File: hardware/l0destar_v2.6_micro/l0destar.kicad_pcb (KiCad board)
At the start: 4 copper layers, 65.4 x 34.4 mm, 75 parts

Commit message: added v2.6C board, minor silkscreen tweaks to other PCBs
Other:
- board text removed: "120Ω"
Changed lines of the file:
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@@
 		)
 	)
-	(gr_text "120Ω"
-		(at 56.22 78 0)
+	(gr_text "GND"
+		(at 31.53 93.58 90)
 		(layer "B.SilkS")
 		(effects
@@
 				(size 0.8 0.8)
 				(thickness 0.15)
-				(bold yes)
 			)
 			(justify left bottom mirror)
+		)
+	)
+	(gr_text "4.2V"
+		(at 31.53 96.1 90)
+		(layer "B.SilkS")
+		(effects
+			(font
+				(size 0.8 0.8)
+				(thickness 0.15)
+			)
+			(justify left bottom mirror)

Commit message: minor PCB layout tweaks
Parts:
- moved S13D1 17.3 mm to (81.0, 106.2), turned to 90 degrees
- moved S13D2 17.3 mm to (82.7, 106.2), turned to 90 degrees
- moved S13D3 17.3 mm to (84.3, 106.2), turned to 90 degrees
- moved S13R1 12.1 mm to (76.4, 103.7), turned to 180 degrees
- moved S13R2 11.2 mm to (76.4, 102.7), turned to 180 degrees
- moved S13R3 10.5 mm to (76.4, 101.6), turned to 180 degrees
- moved H4 1.38 mm to (88.0, 106.3)
- moved H2 1.34 mm to (71.8, 77.2)
- moved S15C1 1.29 mm to (79.8, 81.2)
- moved S15C3 1.29 mm to (78.9, 85.0)
- moved S15FB1 1.29 mm to (77.8, 85.0)
- moved S15J1 1.29 mm to (76.6, 80.7)
- moved S15U1 1.29 mm to (75.0, 85.0)
- moved S15C2 1.29 mm to (80.0, 85.0)
- moved S15C4 1.29 mm to (81.1, 85.0)
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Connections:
- S1J2 pad 18: unconnected-(S1J2-Pin_18-Pad18) -> LED3
- S1J2 pad 19: unconnected-(S1J2-Pin_19-Pad19) -> LED2
- S1J2 pad 20: unconnected-(S1J2-Pin_20-Pad20) -> LED1
- S1J3 pad 21: LED1 -> unconnected-(S1J3-Pin_20-Pad21)
- S1J3 pad 22: LED2 -> unconnected-(S1J3-Pin_19-Pad22)
- S1J3 pad 23: LED3 -> unconnected-(S1J3-Pin_18-Pad23)
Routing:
- net Net-(S13D3-A): track 15.3 -> 8.93 mm
- net Net-(S13D2-A): track 12.2 -> 6.88 mm
- net GND: track 76.6 -> 71.9 mm, vias 125 -> 127
- net Net-(S13D1-A): track 8.79 -> 4.83 mm
- net LED3: track 3.32 -> 6.76 mm
- net PP3V3_GPS: track 19.0 -> 20.3 mm
- net LED2: track 3.21 -> 4.44 mm
- net PP3V3_AUX: track 23.2 -> 24.2 mm
- net LED1: track 3.04 -> 2.51 mm
- net unconnected-(S1J3-Pin_19-Pad22): track 0.00 -> 0.51 mm
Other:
- board size 65.4 x 34.4 mm -> 66.8 x 34.4 mm

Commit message: tweaked layouts
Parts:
- removed S1R3: 100K, Resistor_SMD:R_0402_1005Metric
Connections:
- S1J2 pad 2: VSYS -> unconnected-(S1J2-VSYS-Pad2)
- S1J2 pad 4: Net-(S1J2-ENABLE) -> unconnected-(S1J2-ENABLE-Pad4)
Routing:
- net Net-(S1J2-ENABLE): track 3.54 -> 0.00 mm
- net VSYS: track 3.07 -> 0.00 mm
- net GND: track 71.9 -> 71.6 mm, vias 127 -> 113
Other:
- board text removed: "ENABLE"
- board text removed: "VSYS"

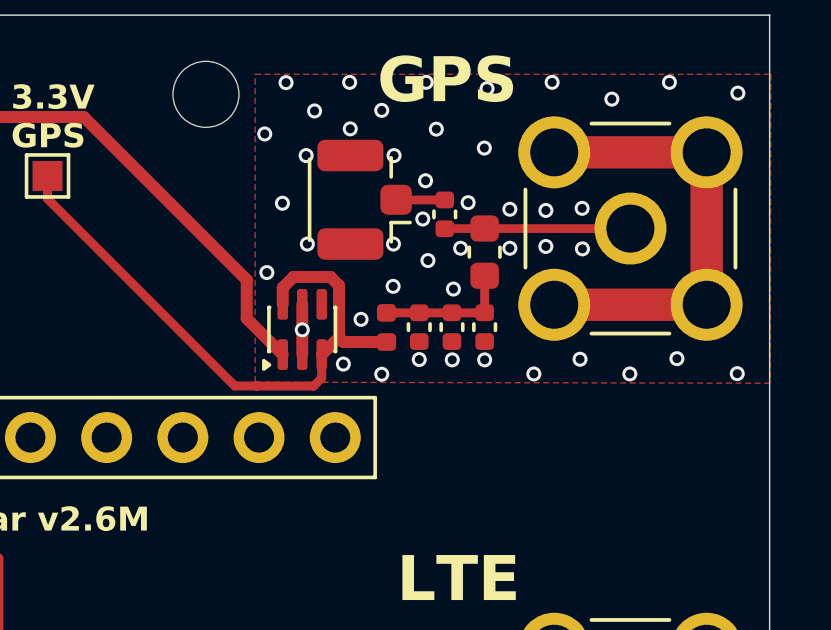
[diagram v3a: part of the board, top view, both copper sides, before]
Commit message: fix bias tee cap ordering on all boards
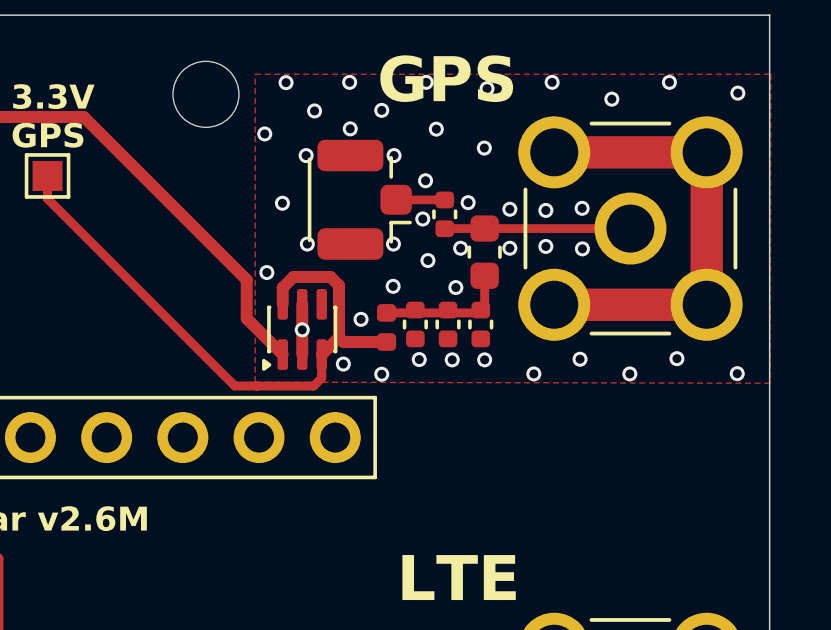
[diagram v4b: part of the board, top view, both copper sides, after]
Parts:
- moved S15C4 2.31 mm to (78.8, 84.9)
- moved S15C2 0.96 mm to (81.0, 84.9)
- moved S15C3 0.96 mm to (79.9, 84.9)
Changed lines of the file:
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@@
 	(footprint "Capacitor_SMD:C_0402_1005Metric"
 		(layer "F.Cu")
-		(at 78.9 84.97 -90)
+		(at 79.86 84.88 -90)
 		(descr "Capacitor SMD 0402 (1005 Metric), square (rectangular) end terminal, IPC-7351 nominal, (Body size source: IPC-SM-782 page 76, https://www.pcb-3d.com/wordpress/wp-content/uploads/ipc-sm-782a_amendment_1_and_2.pdf)")
 		(tags "capacitor")
@@
 	(footprint "Capacitor_SMD:C_0402_1005Metric"
 		(layer "F.Cu")
-		(at 79.99 84.97 -90)
+		(at 80.95 84.88 -90)
 		(descr "Capacitor SMD 0402 (1005 Metric), square (rectangular) end terminal, IPC-7351 nominal, (Body size source: IPC-SM-782 page 76, https://www.pcb-3d.com/wordpress/wp-content/uploads/ipc-sm-782a_amendment_1_and_2.pdf)")
 		(tags "capacitor")
@@
 	(footprint "Capacitor_SMD:C_0402_1005Metric"
 		(layer "F.Cu")
-		(at 81.08 84.97 -90)
+		(at 78.77 84.88 -90)
 		(descr "Capacitor SMD 0402 (1005 Metric), square (rectangular) end terminal, IPC-7351 nominal, (Body size source: IPC-SM-782 page 76, https://www.pcb-3d.com/wordpress/wp-content/uploads/ipc-sm-782a_amendment_1_and_2.pdf)")
 		(tags "capacitor")
@@
 	)
 	(via
-		(at 80.04 83.7)
+		(at 80.12 83.65)
 		(size 0.5)
 		(drill 0.3)
